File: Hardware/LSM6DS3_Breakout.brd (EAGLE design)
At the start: 22.9 x 22.9 mm, 25 parts, among them U2 LSM6DS3

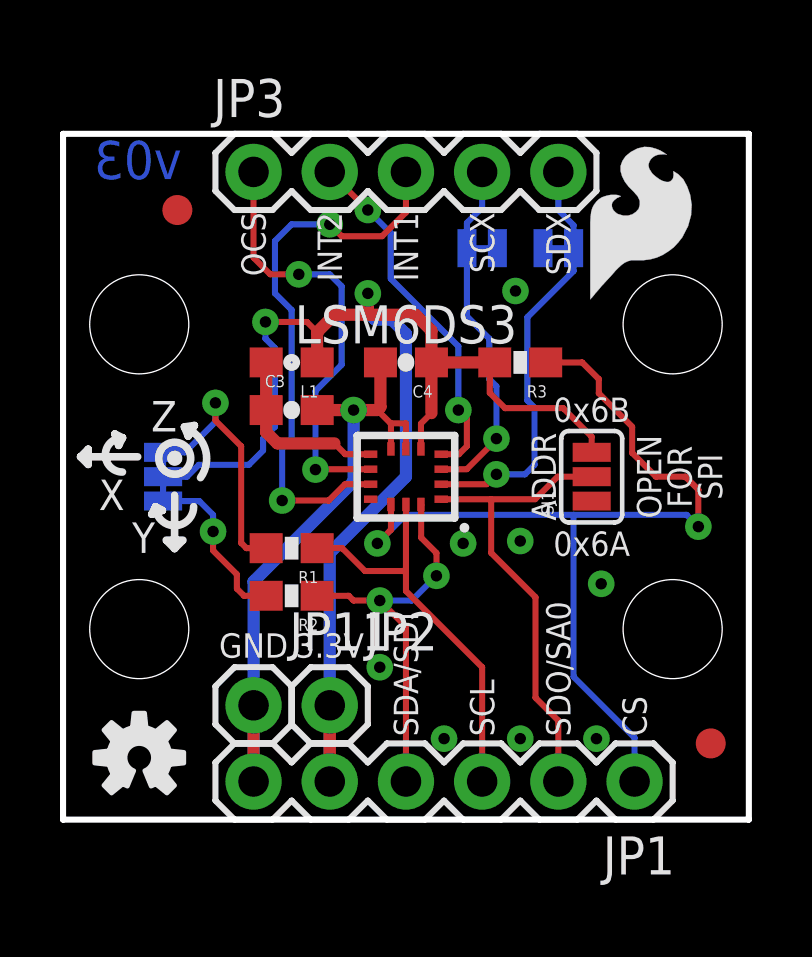
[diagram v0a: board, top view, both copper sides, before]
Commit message: Fixed silk for redboards
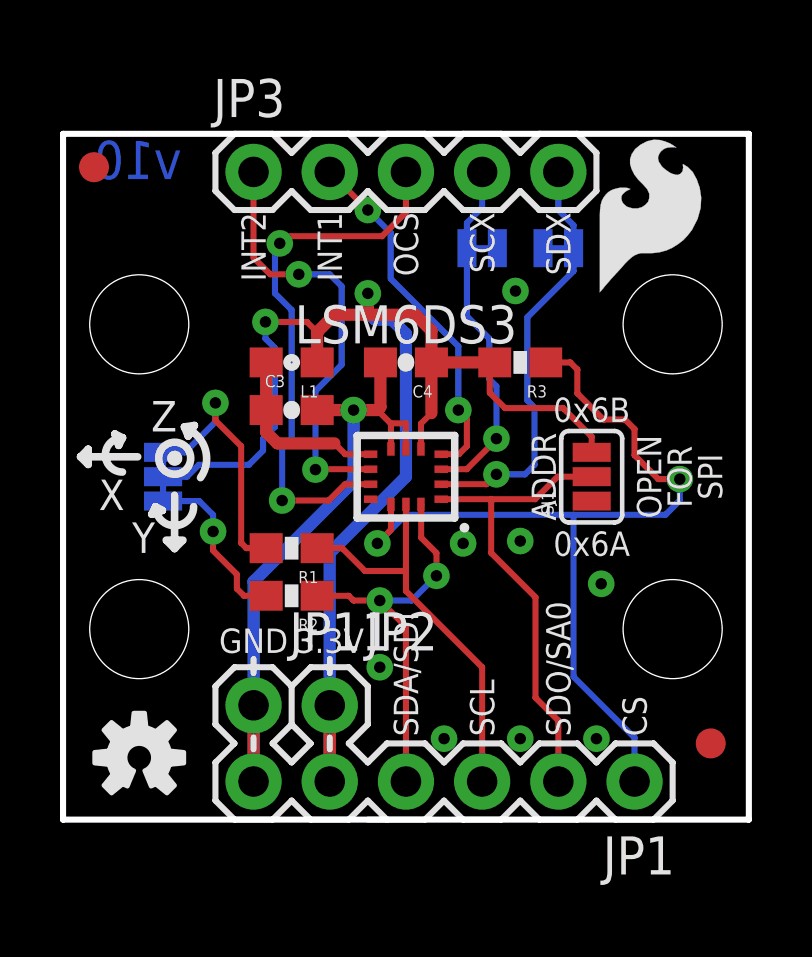
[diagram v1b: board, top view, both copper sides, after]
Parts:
- JP1: device SparkFun-Connectors:1X06 -> SparkFun-Connectors:1X06_NO_SILK_YES_STOP
- JP11, JP2: device SparkFun-Connectors:1X01 -> SparkFun-Connectors:1X01_NO_SILK
- moved FID1 3.12 mm to (1.03, 21.7)
- moved LOGO1 0.40 mm to (17.5, 17.3)
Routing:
- net CS: track 31.4 -> 29.7 mm
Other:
- board text added: "v10"
- board text removed: "v03"
